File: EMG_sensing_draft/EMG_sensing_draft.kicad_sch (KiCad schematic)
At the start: 54 parts, among them J1 EMG_SIGNAL, J2 USB_A_0480370001, J3 DEBUG, U1 W25Q128JV, U2 RN4871-I/RM140, U3 RP2040, U4 OPAMP, U5 MCP1702T-3302E_CB, U6 OPAMP, U7 OPAMP, U8 MCP6N11-002E/SN, U9 OPAMP, Y1 12MHz

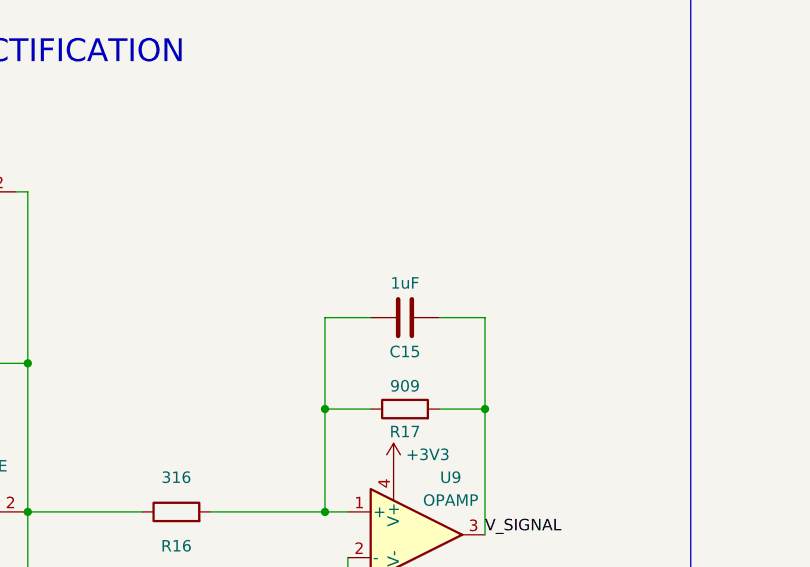
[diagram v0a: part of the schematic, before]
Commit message: Update after design review
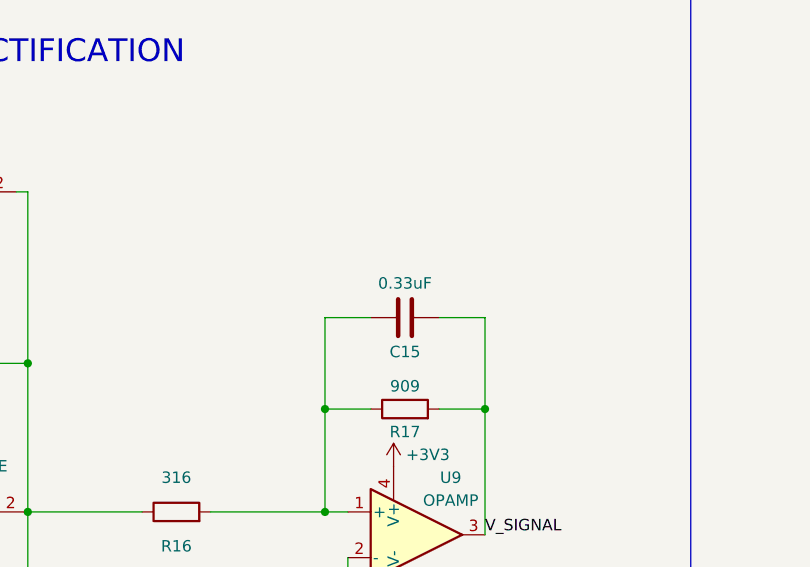
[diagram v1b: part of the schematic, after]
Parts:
- C15: value 1uF -> 0.33uF
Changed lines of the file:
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@@
     (in_bom yes) (on_board yes)
     (property "Reference" "C15" (id 0) (at 314.96 110.49 90))
-    (property "Value" "1uF" (id 1) (at 314.96 102.87 90))
+    (property "Value" "0.33uF" (id 1) (at 314.96 102.87 90))
     (property "Footprint" "" (id 2) (at 318.77 105.7148 0)
       (effects (font (size 1.27 1.27)) hide)
@@
     )
     (path "/0392a271-4134-41ca-8350-e6e1460a370e"
-      (reference "C15") (unit 1) (value "1uF") (footprint "")
+      (reference "C15") (unit 1) (value "0.33uF") (footprint "")
     )
     (path "/edc6d0d1-95cd-4bd8-8476-e09b97bf0890"

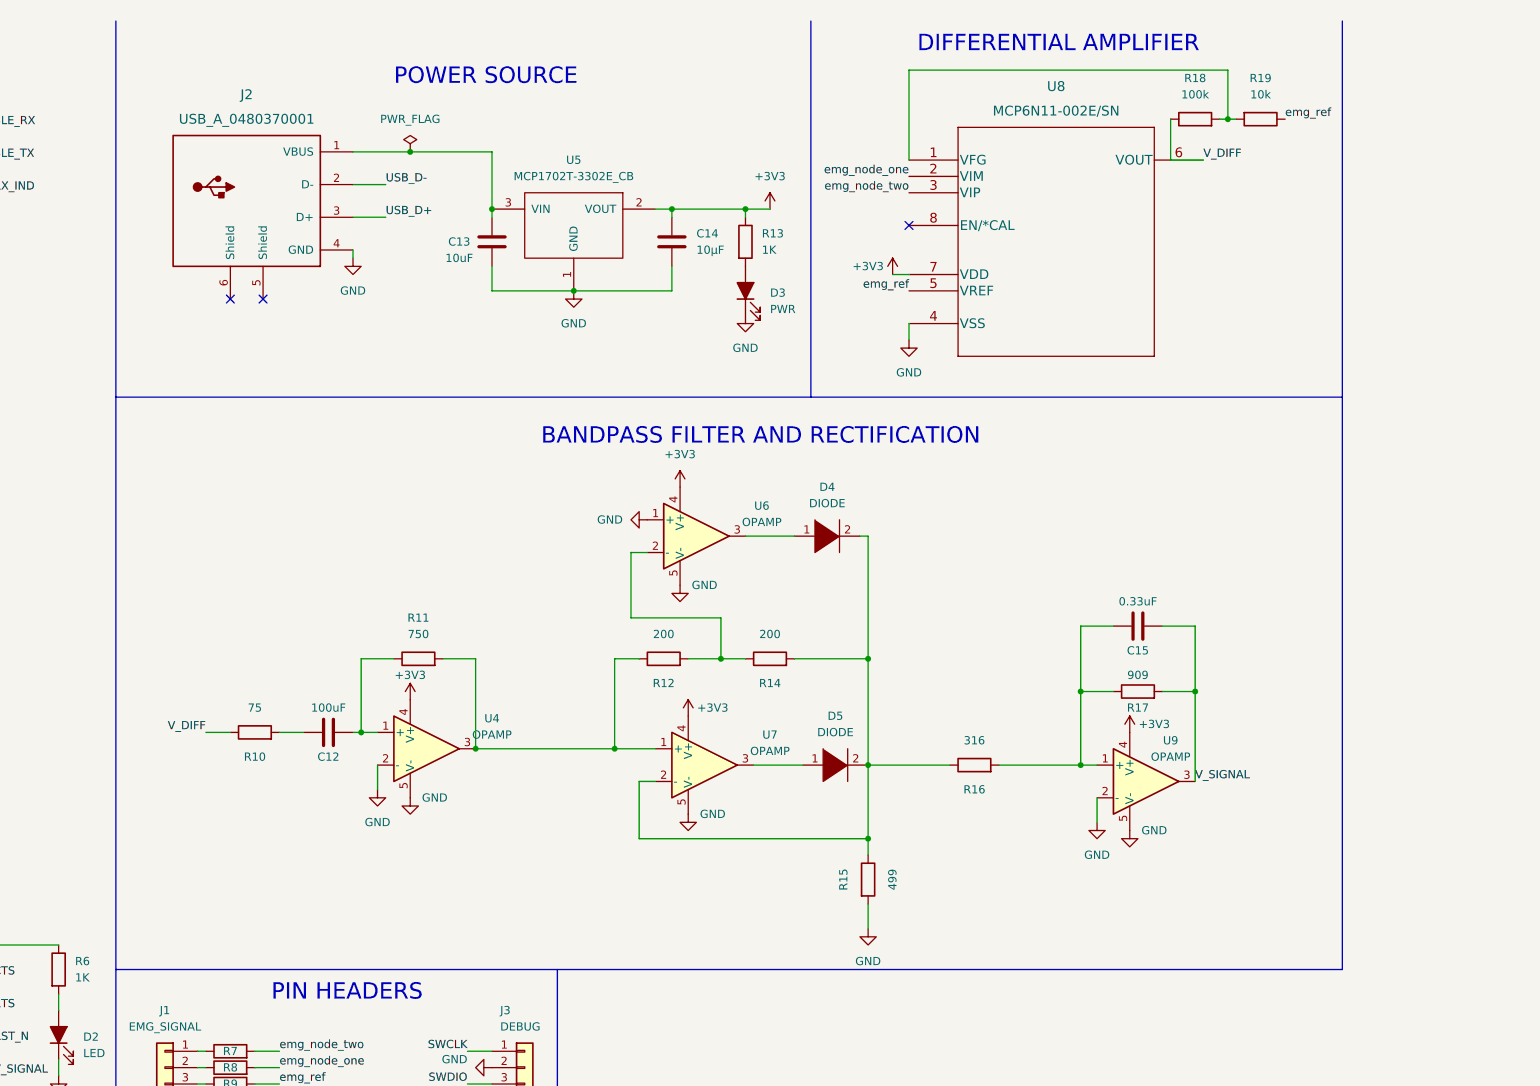
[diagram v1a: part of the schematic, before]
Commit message: Update circuit based on Brad's advice
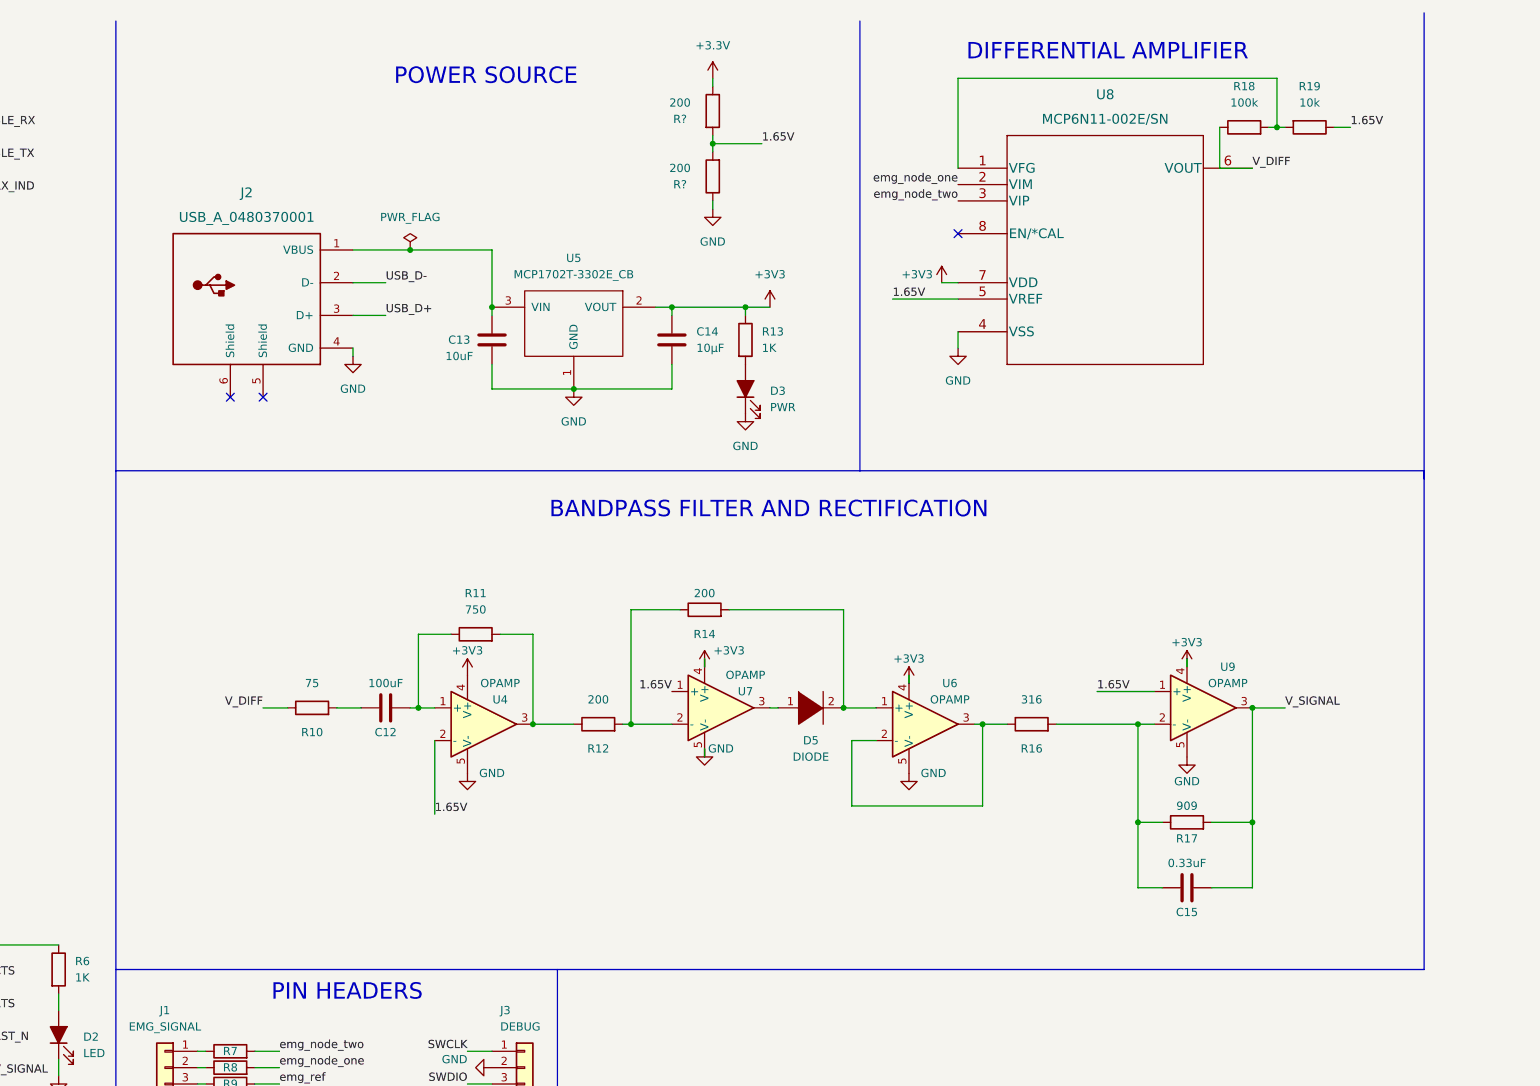
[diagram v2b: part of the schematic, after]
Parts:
- removed D4: DIODE, symbol pspice:DIODE
- removed R15: 499, symbol Device:R
- added R? (x2): 200, symbol Device:R
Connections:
- net GND: now also R?.1; no longer U4.2 (-), U6.1 (+), U9.2 (-)
- net emg_ref: no longer R19.1, U8.5 (VREF)
- net at C15.1, R16.2, R17.1: now also U9.2 (-); no longer U9.1 (+)
- net at R12.2, R14.1: now also U7.2 (-); no longer U6.2 (-)
- net at D5.2 (A), R14.2: now also U6.1 (+); no longer R16.1, U7.2 (-)
- net at R11.2, R12.1, U4.3: no longer U7.1 (+)
- net at U6.3: now also R16.1, U6.2 (-)
- new net +3.3V: R?.1
- new net 1.65V: R19.1, R?.2, R?.2, U4.2 (-), U7.1 (+), U8.5 (VREF), U9.1 (+)
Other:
- moved on the sheet: C12, C13, C14, C15, D3, D5, J2, R10, R11, R12, R13, R14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

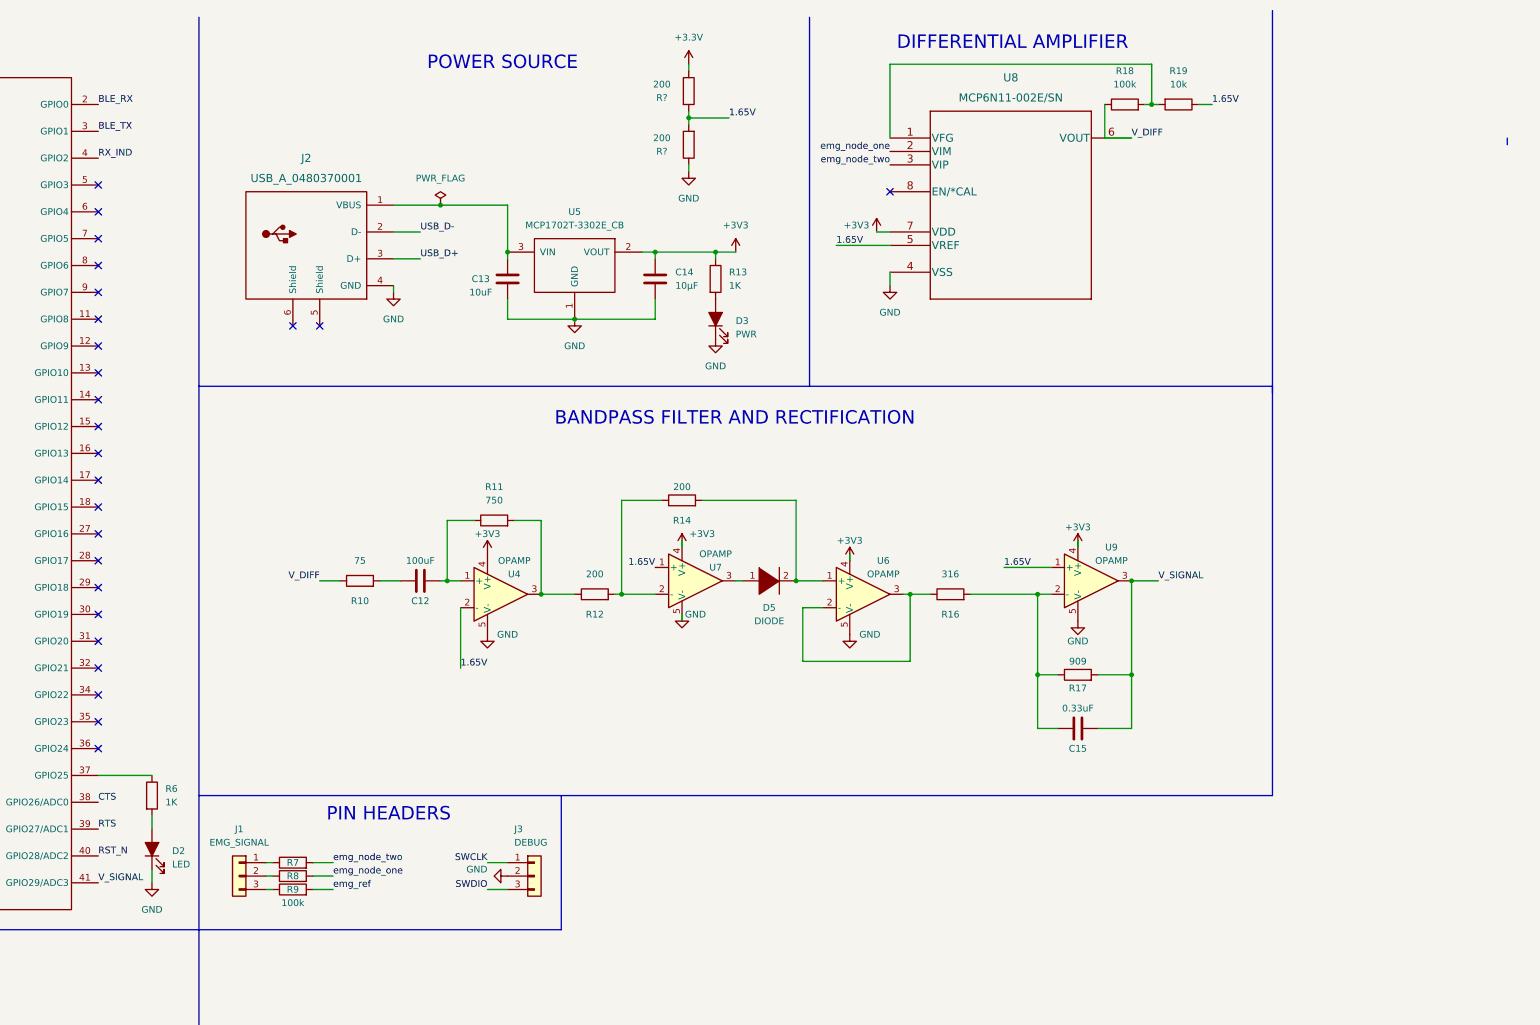
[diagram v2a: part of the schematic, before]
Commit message: Change opamp chip and add bypass
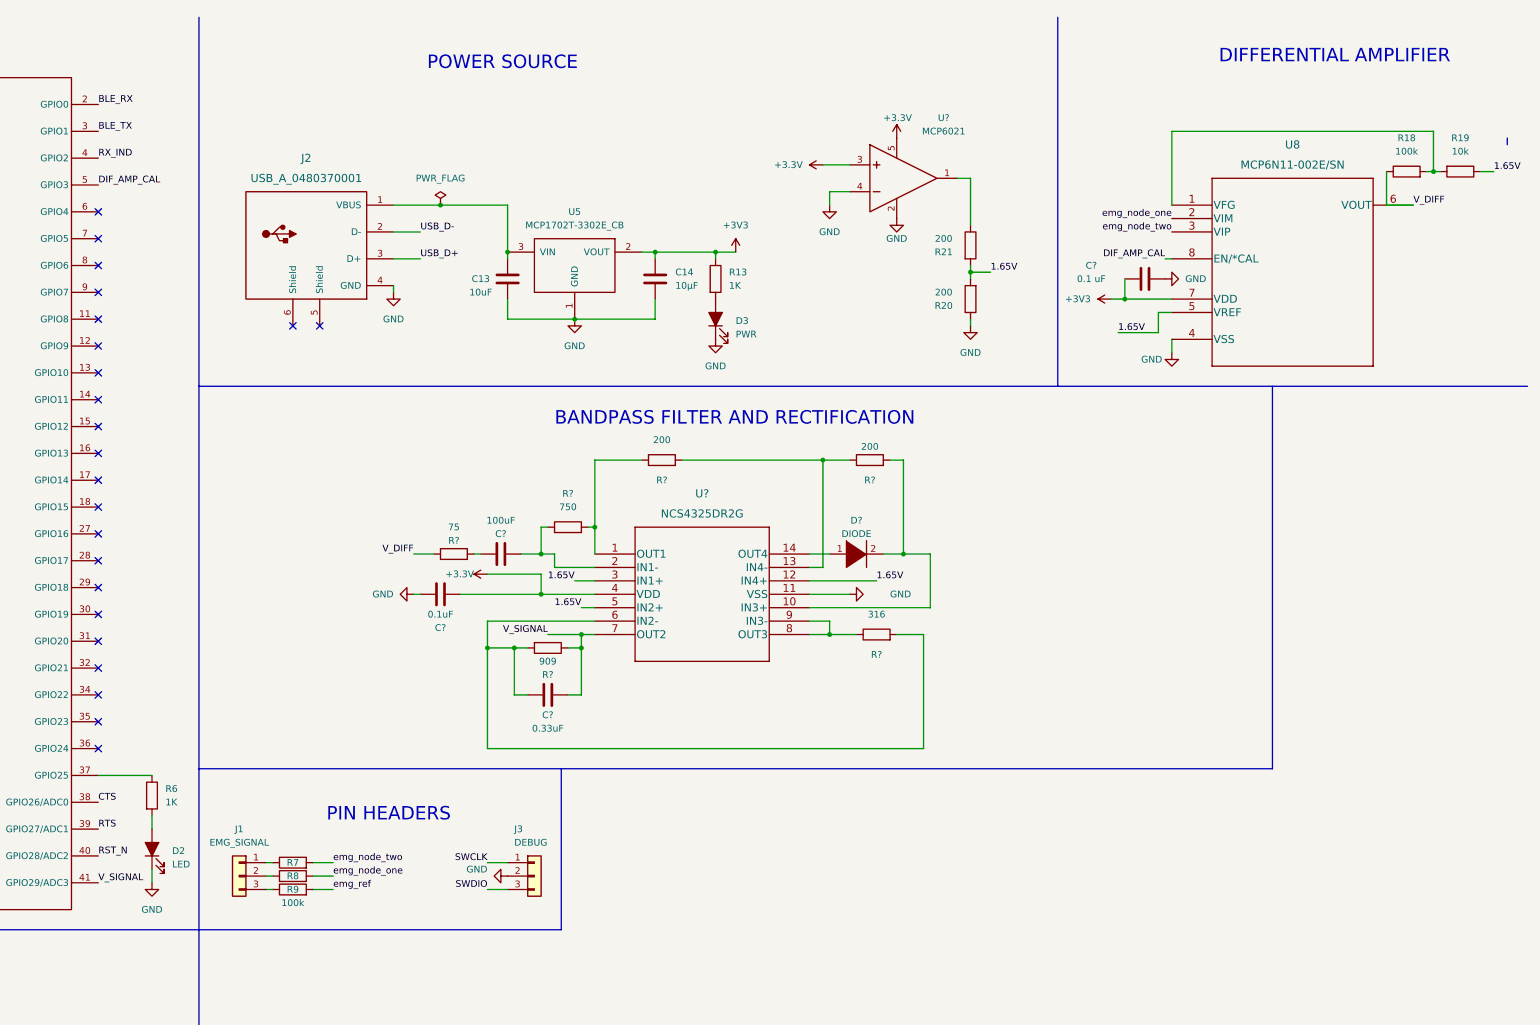
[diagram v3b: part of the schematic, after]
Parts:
- removed C12: 100uF, symbol Device:C
- removed C15: 0.33uF, symbol Device:C
- removed D5: DIODE, symbol pspice:DIODE
- removed R10: 75, symbol Device:R
- removed R11: 750, symbol Device:R
- removed R12, R14: 200, symbol Device:R
- removed R16: 316, symbol Device:R
- removed R17: 909, symbol Device:R
- removed U4, U6, U7, U9: OPAMP, symbol pspice:OPAMP
- added C?: 100uF, symbol Device:C
- added C?: 0.1 uF, symbol Device:C
- added C?: 0.33uF, symbol Device:C
- added C?: 0.1uF, symbol Device:C
- added D?: DIODE, symbol pspice:DIODE
- added R? (x2): 200, symbol Device:R
- added R?: 75, symbol Device:R
- added R?: 750, symbol Device:R
- added R?: 316, symbol Device:R
- added R?: 909, symbol Device:R
- added U?: MCP6021, symbol Eclectronics:MCP6021
- added U?: NCS4325DR2G, SOIC14_4X8P75_ONS, symbol NCS4325DR2G:NCS4325DR2G
- gave numbers to parts that had none: 2
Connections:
- net +3.3V: now also C?.2, U?.3, U?.4 (VDD), U?.5; no longer R21.1
- net +3V3: now also C?.1
- net 1.65V: now also U?.12 (IN4+), U?.3 (IN1+), U?.5 (IN2+)
- net GND: now also C?.1, C?.2, U?.11 (VSS), U?.2, U?.4
- net V_DIFF: now also R?.1
- net V_SIGNAL: now also C?.2, R?.1, U?.7 (OUT2)
- net DIF_AMP_CAL: now reaches U3.5 (GPIO3)
- net DIF_AMP_CAL: now also U8.8 (EN/*CAL)
- new net: R?.1, R?.2, U?.1 (OUT1)
- new net: R?.1, R?.2, U?.13 (IN4-)
- new net: D?.1 (K), U?.14 (OUT4)
- new net: D?.2 (A), R?.2, U?.10 (IN3+)
- new net: C?.1, R?.2
- new net: C?.2, R?.1, U?.2 (IN1-)
- new net: C?.1, R?.2, R?.2, U?.6 (IN2-)
- new net: R21.1, U?.1
- new net: R?.1, U?.8 (OUT3), U?.9 (IN3-)
- no-connect marks 30 -> 28
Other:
- moved on the sheet: R18, R19, R20, R21, U8

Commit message: Fix diode
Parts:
- removed D?: DIODE, symbol pspice:DIODE
- added D4: DIODE, symbol Simulation_SPICE:DIODE
- gave numbers to parts that had none: 12
- renumbered C13 to C14, C14 to C16, R13 to R14, R21 to R17, R20 to R18, R18 to R19, R19 to R20, U5 to U4, U8 to U7
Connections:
- net at U5.14 (OUT4): now also D4.1 (A)
- net at R15.2, U5.10 (IN3+): now also D4.2 (K)

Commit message: Update circuit w new resistor values
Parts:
- C13: value 100uF -> 10uF
- R10: value 75 -> 787
- R12: value 750 -> 8.1K
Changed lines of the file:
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@@
     (in_bom yes) (on_board yes)
     (property "Reference" "C13" (id 0) (at 213.36 110.49 90))
-    (property "Value" "100uF" (id 1) (at 213.36 107.95 90))
+    (property "Value" "10uF" (id 1) (at 213.36 107.95 90))
     (property "Footprint" "" (id 2) (at 217.17 113.3348 0)
       (effects (font (size 1.27 1.27)) hide)
@@
     (in_bom yes) (on_board yes)
     (property "Reference" "R10" (id 0) (at 204.47 111.76 90))
-    (property "Value" "75" (id 1) (at 204.47 109.22 90))
+    (property "Value" "787" (id 1) (at 204.47 109.22 90))
     (property "Footprint" "" (id 2) (at 204.47 116.078 90)
       (effects (font (size 1.27 1.27)) hide)
@@
     (in_bom yes) (on_board yes) (fields_autoplaced)
     (property "Reference" "R12" (id 0) (at 226.06 102.87 90))
-    (property "Value" "750" (id 1) (at 226.06 105.41 90))
+    (property "Value" "8.1K" (id 1) (at 226.06 105.41 90))
     (property "Footprint" "" (id 2) (at 226.06 110.998 90)
       (effects (font (size 1.27 1.27)) hide)
@@
     )
     (path "/119c3aed-e25b-451b-8a41-ecdd441151c4"
-      (reference "C13") (unit 1) (value "100uF") (footprint "")
+      (reference "C13") (unit 1) (value "10uF") (footprint "")
     )
     (path "/2d833c17-71e7-42c7-b9f3-0c31cf2e96e2"
@@
     )
     (path "/34542205-bb26-439b-be2b-5c4fef448fd0"
-      (reference "R10") (unit 1) (value "75") (footprint "")
+      (reference "R10") (unit 1) (value "787") (footprint "")
     )
     (path "/dd22e7d4-d6e6-4fad-9fda-5ede9dd844e7"
@@
     )
     (path "/5da1655c-58a9-4fc6-bcf4-7a6ba7b254d9"
-      (reference "R12") (unit 1) (value "750") (footprint "")
+      (reference "R12") (unit 1) (value "8.1K") (footprint "")
     )
     (path "/082d5159-8617-4ea9-8e71-abc836cf9dc0"

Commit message: added power symbol and cleaned up schematic
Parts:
- removed R20: 10k, symbol Device:R
- added C17, C19: 1uF, symbol Device:C
- added C18: .1uF, symbol Device:C
- added D2, D3, D4: LED, LED_SMD:LED_0805_2012Metric, symbol Device:LED_Filled
- added R23: 10k, symbol Device:R
- added R6, R7, R8: 1K, Resistor_SMD:R_0402_1005Metric, symbol Device:R
- C20: renamed from C17; value 0.1 uF -> 0.1uF
- R20: renamed from R17; value 200 -> 10k
- R21: renamed from R18; value 200 -> 10k
- renumbered D2 to D5, D3 to D6, D4 to D7, R7 to R10, R8 to R11, R9 to R12, R10 to R13, R11 to R14, R12 to R15, R13 to R16, R14 to R17, R15 to R18, R16 to R19, R19 to R22, R6 to R9
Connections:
- net +3V3 is gone; now on net +3.3V: C1.2, C16.1, C2.1, C20.1, C3.1, C4.1, C5.1, C6.1, C7.1, C8.1, D1.2 (A), R1.2, R17.1, R2.2, U1.8 (VDD), U2.14 (VBAT), U3.1 (IOVDD), U3.10 (IOVDD), U3.22 (IOVDD), U3.33 (IOVDD), U3.42 (IOVDD), U3.43 (ADC_AVDD), U3.44 (VREG_VIN), U3.48 (USB_VDD), U3.49 (IOVDD), U4.2 (VOUT), U7.7 (VDD)
- net +3.3V: now also C17.1, C18.1, C19.1
- net CTS: now also U3.5 (GPIO3); no longer U3.38 (GPIO26/ADC0)
- net DIF_AMP_CAL: now also U3.8 (GPIO6); no longer U3.5 (GPIO3)
- net GND: now also C17.2, C18.2, C19.2, D2.1 (K), D3.1 (K), D4.1 (K); no longer U6.4, U7.4 (VSS)
- net RST_N: now also U3.7 (GPIO5); no longer U3.40 (GPIO28/ADC2)
- net RTS: now also U3.6 (GPIO4); no longer U3.39 (GPIO27/ADC1)
- net emg_ref: now also U7.4 (VSS)
- net at U3.34 (GPIO22): now also R6.1
- net at U3.35 (GPIO23): now also R7.1
- net at U3.36 (GPIO24): now also R8.1
- net at R20.1, U6.1: now also U6.4
- net at R22.2, U7.1 (VFG): now also R23.1
- net 1.65V renamed +1.65V
- net +1.65V: now also R23.2
- new net: D3.2 (A), R7.2
- new net: D2.2 (A), R6.2
- new net: D4.2 (A), R8.2
- no-connect marks 28 -> 25
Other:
- moved on the sheet: C12, C20, D5, R22, R9, U6, U7
